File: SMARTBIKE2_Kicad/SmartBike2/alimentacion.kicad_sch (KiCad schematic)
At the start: 9 parts, among them J1 Conn_01x02, U1 MIC29302WU

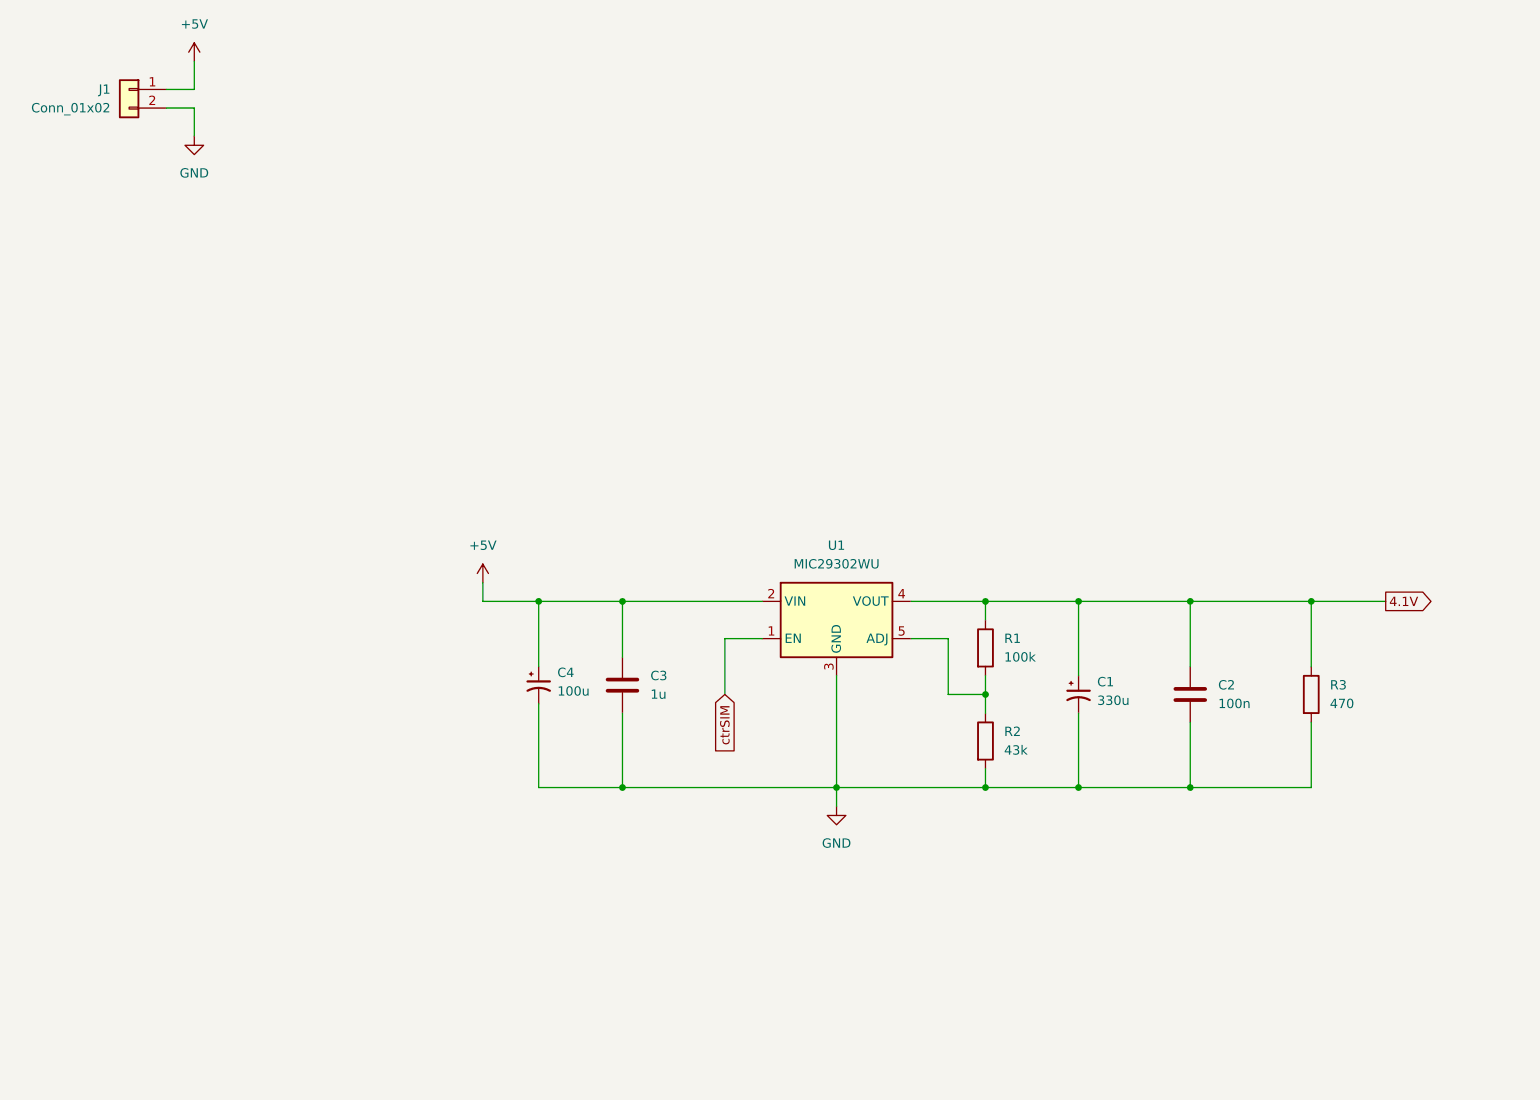
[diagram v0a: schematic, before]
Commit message: Alimentación ESP32
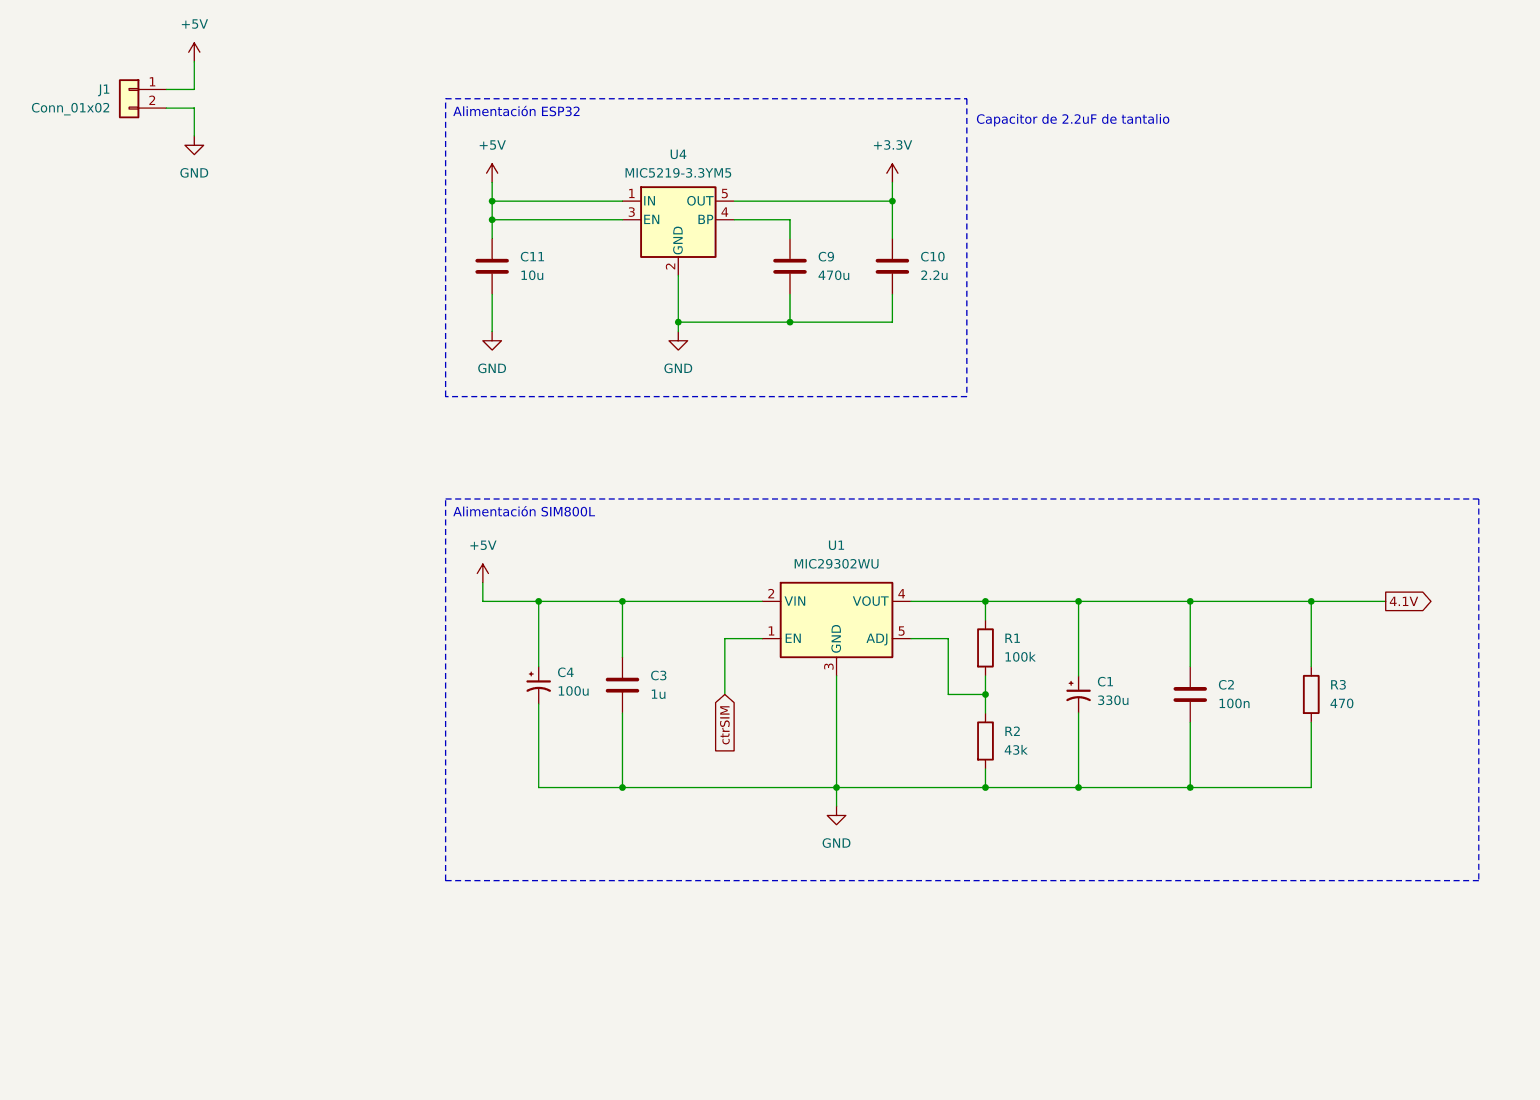
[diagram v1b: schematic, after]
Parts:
- added C10: 2.2u, symbol Device:C
- added C11: 10u, symbol Device:C
- added C9: 470u, symbol Device:C
- added U4: MIC5219-3.3YM5, Package_TO_SOT_SMD:SOT-23-5, symbol Regulator_Linear:MIC5219-3.3YM5
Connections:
- net +5V: now also C11.1, U4.1 (IN), U4.3 (EN)
- net GND: now also C10.2, C11.2, C9.2, U4.2 (GND)
- new net: C9.1, U4.4 (BP)
- new net +3.3V: C10.1, U4.5 (OUT)
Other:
- note added: "Capacitor de 2.2uF de tantalio"

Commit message: Alarma, luces frontales y modulos
+ Circuito luces frontales
+ Conector Luces
+ Conector GPS
+ Conector SIM
+ Conector acelerómetro

~ Acondicionamiento ESP32
~ Huellas
~ PCB
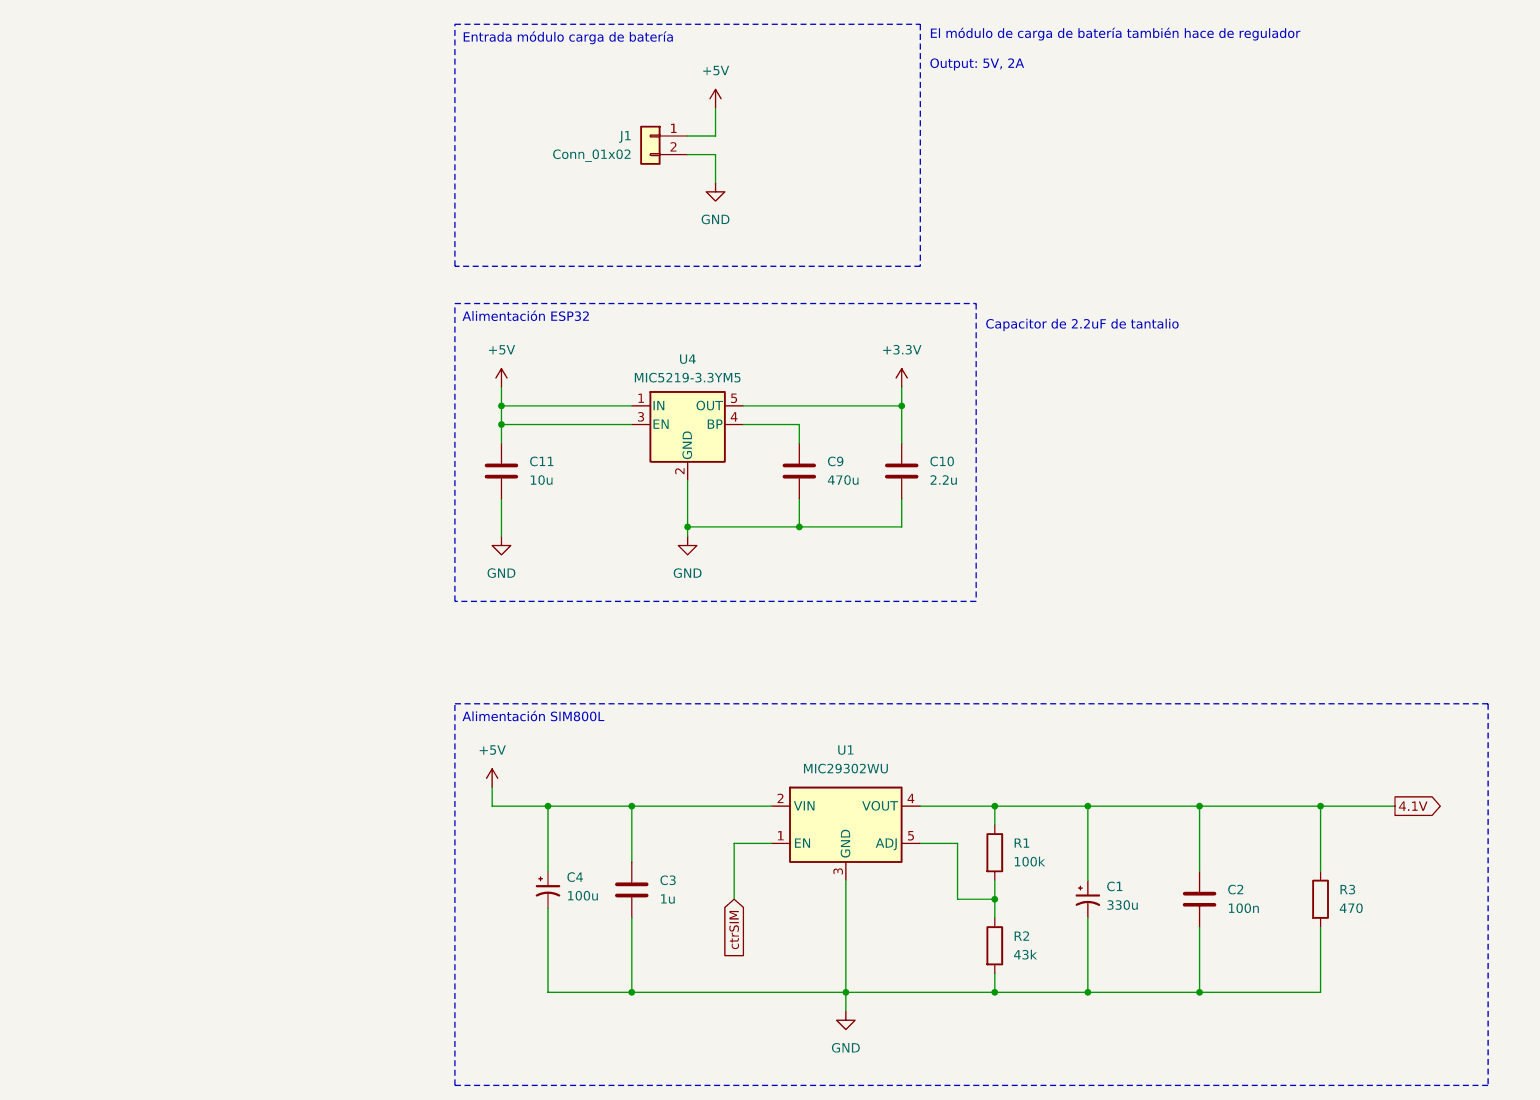
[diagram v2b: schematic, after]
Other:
- note added: "El módulo de carga de batería también hace de regulador Output: 5V, 2A"
- moved on the sheet: C1, C10, C11, C2, C3, C4, C9, J1, R1, R2, R3, U1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

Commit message: Beta 100% esquemáticos
+ Acondicionamiento ESP32

~ Huellas
~ PCB
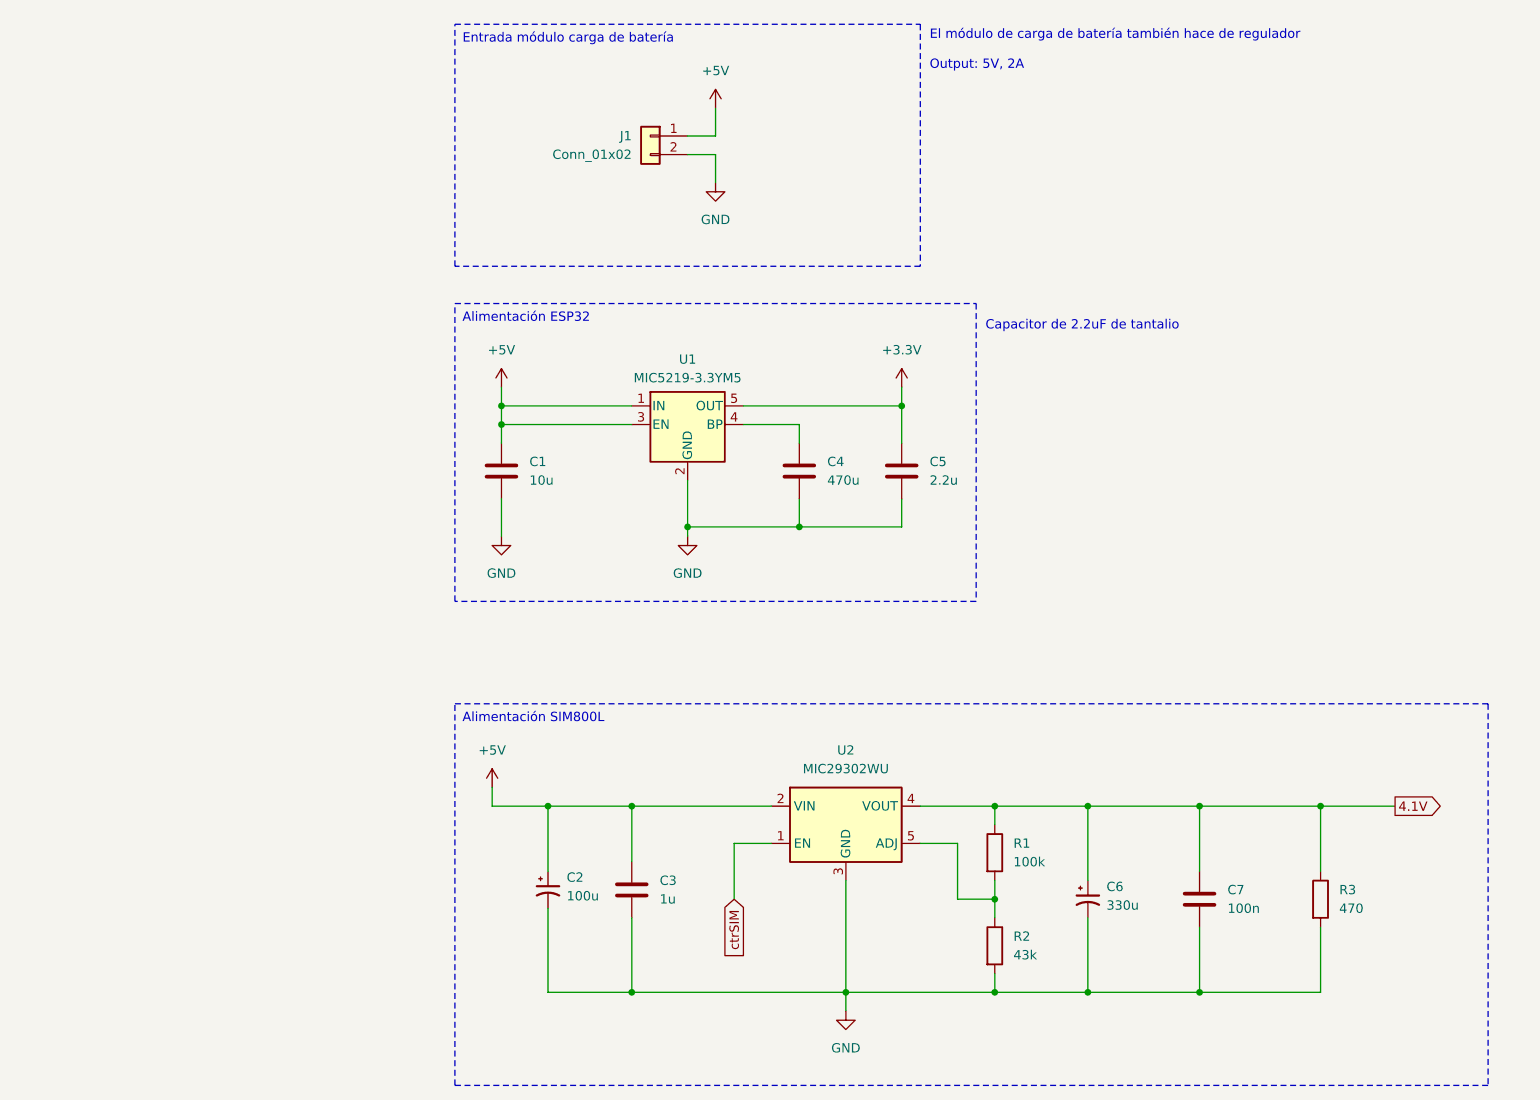
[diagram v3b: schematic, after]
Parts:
- renumbered C11 to C1, C4 to C2, C9 to C4, C10 to C5, C1 to C6, C2 to C7, U4 to U1, U1 to U2

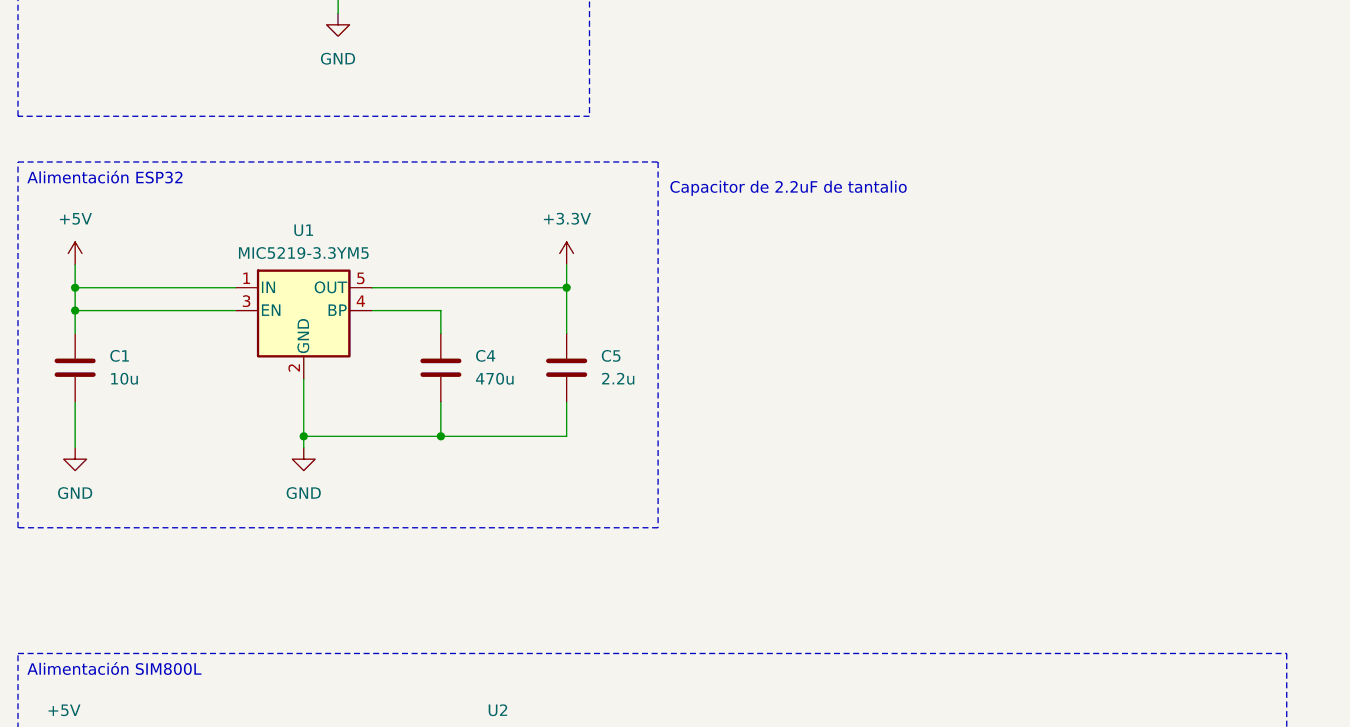
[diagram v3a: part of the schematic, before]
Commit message: cambio alimentacion GPS
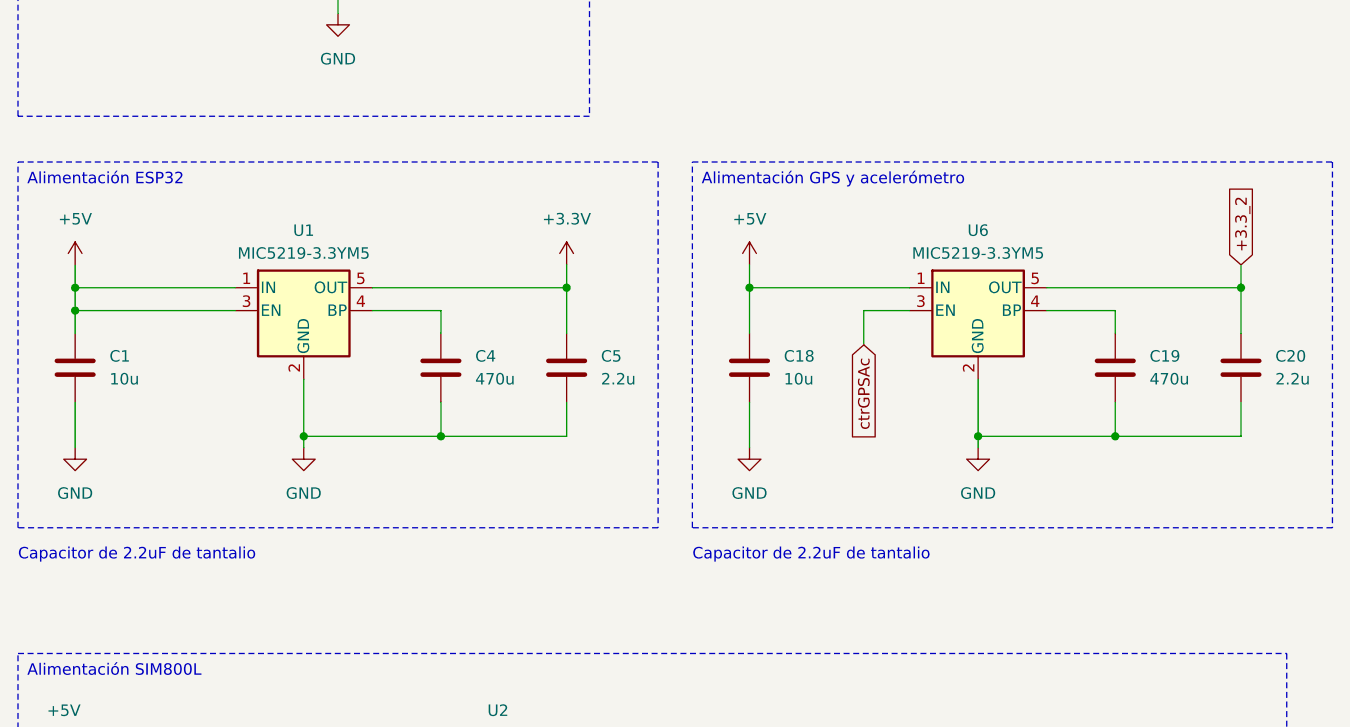
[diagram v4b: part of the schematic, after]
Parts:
- added C18: 10u, symbol Device:C
- added C19: 470u, symbol Device:C
- added C20: 2.2u, symbol Device:C
- added U6: MIC5219-3.3YM5, Package_TO_SOT_SMD:SOT-23-5, symbol Regulator_Linear:MIC5219-3.3YM5
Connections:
- net +5V: now also C18.1, U6.1 (IN)
- net GND: now also C18.2, C19.2, C20.2, U6.2 (GND)
- new net: C19.1, U6.4 (BP)
- new net +3.3_2: C20.1, U6.5 (OUT)
- new net ctrGPSAc: U6.3 (EN)
